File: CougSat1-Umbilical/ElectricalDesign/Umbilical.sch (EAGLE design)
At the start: 40 parts, among them Q1 CSD16406Q3, Q2 CSD16406Q3, U1 FT230XQ, U2 BQ24650

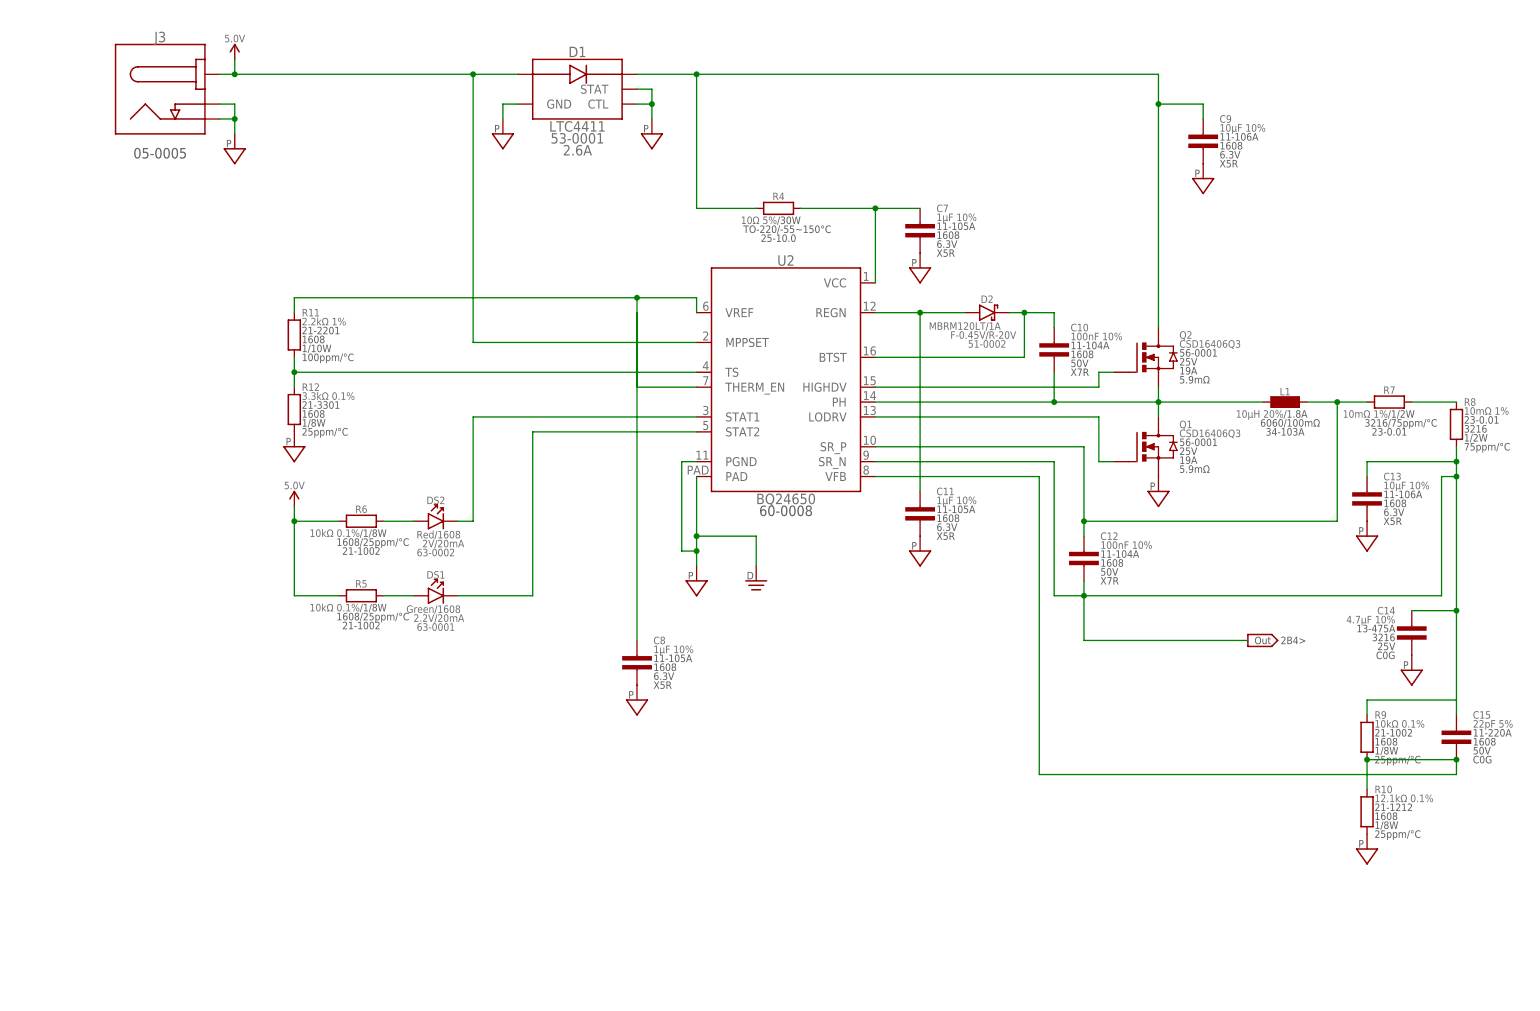
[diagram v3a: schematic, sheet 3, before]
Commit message: Update CougSat1-Umbilical/ElectricalDesign/Umbilical.sch
Fixed typing errors and cleaned up schmatic
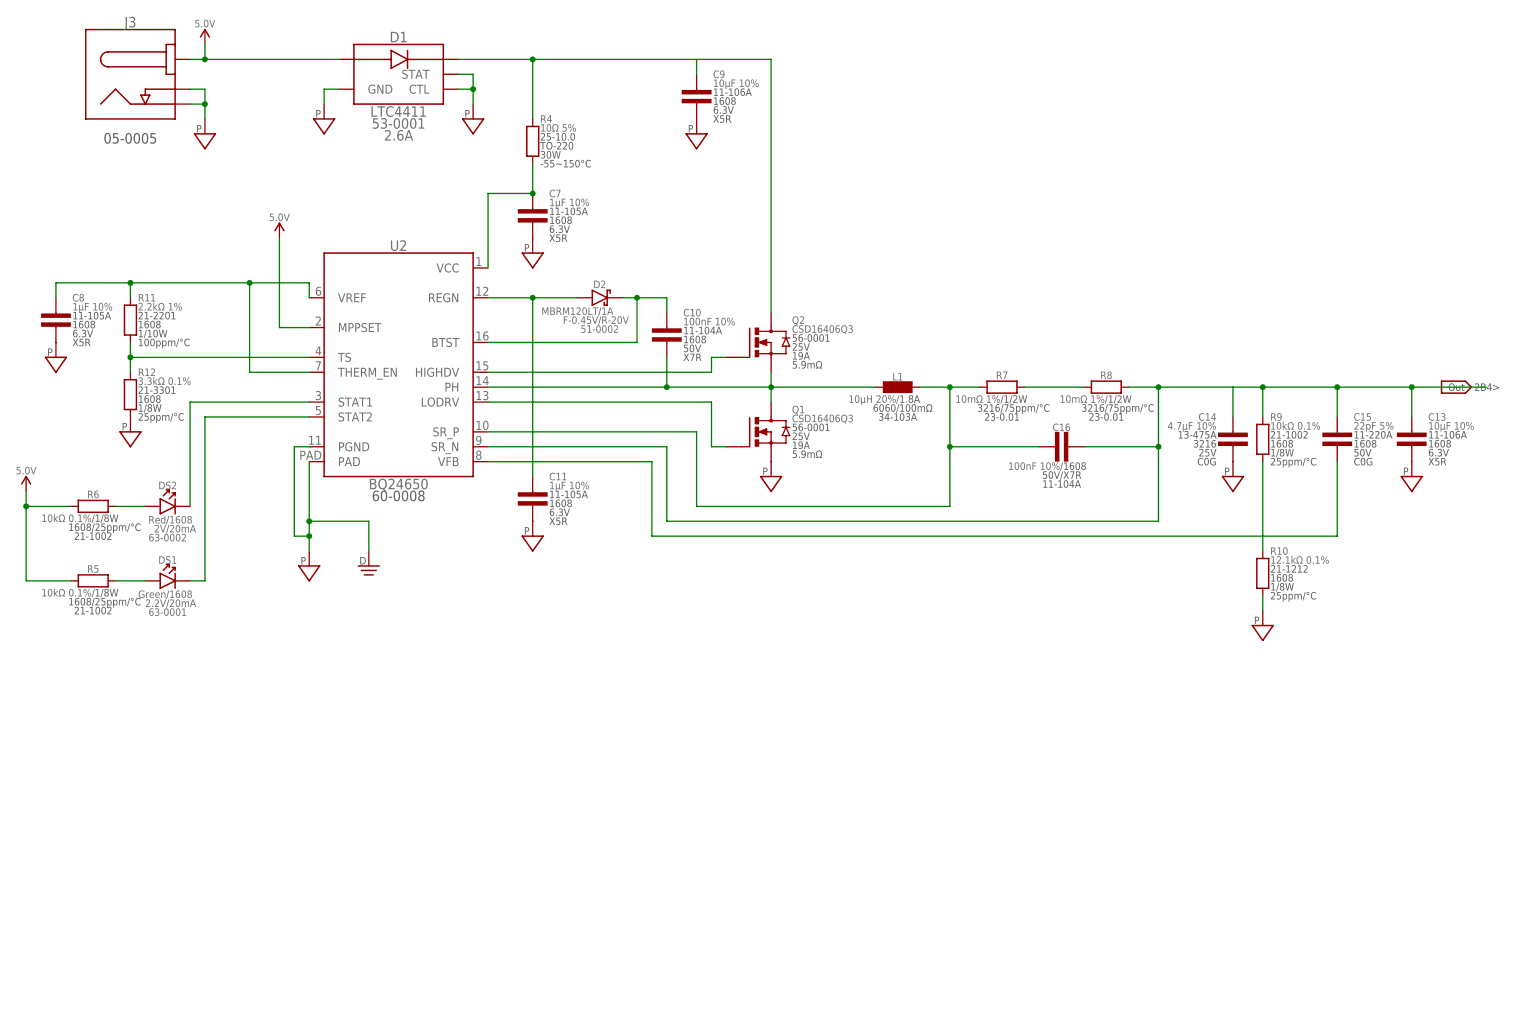
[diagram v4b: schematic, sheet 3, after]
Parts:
- removed C12: 100nF 10%, CougsInSpace-Capacitors:CAP-V-100NF-1608
- added C16: 100nF 10%, CougsInSpace-Capacitors:CAP-H-100NF-1608
- R4: device CougsInSpace-Resistors:RES-H-10R-TO220 -> CougsInSpace-Resistors:RES-V-10R-TO220
- R8: device CougsInSpace-Resistors:RES-V-0.01R-3216 -> CougsInSpace-Resistors:RES-H-0.01R-3216
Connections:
- removed net BARREL_MPPSET: D1.IN, J3.CENTER, U2.MPPSET
- removed net N$14: R7.2, R8.2
- removed net N$3: U2.THERM_EN
- new net N$1: C9.1
- new net N$2: R7.2, R8.1
- new net N$4: R10.2, R9.1
- net 5.0V: now also D1.IN, J3.CENTER, U2.MPPSET
- net BAT_CHARGE_OUT: now also C16.2, R8.2; no longer C12.2, R8.1
- net DIODE_OUT: now also R4.2; no longer C9.1, R4.1
- net SR_P: now also C16.1; no longer C12.1
- net VCC: now also R4.1; no longer R4.2
- net VFB: no longer R10.2, R9.1
- net VREF: now also U2.THERM_EN
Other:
- note added: "3B6>"
- note removed: "3C5>"
- moved on the sheet: C1, C10, C11, C13, C14, C15, C2, C3, C4, C5, C6, C7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

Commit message: Update CougSat1-Umbilical/ElectricalDesign/Umbilical.sch
1.0.1
Cleaned up schematic and changed resistors.
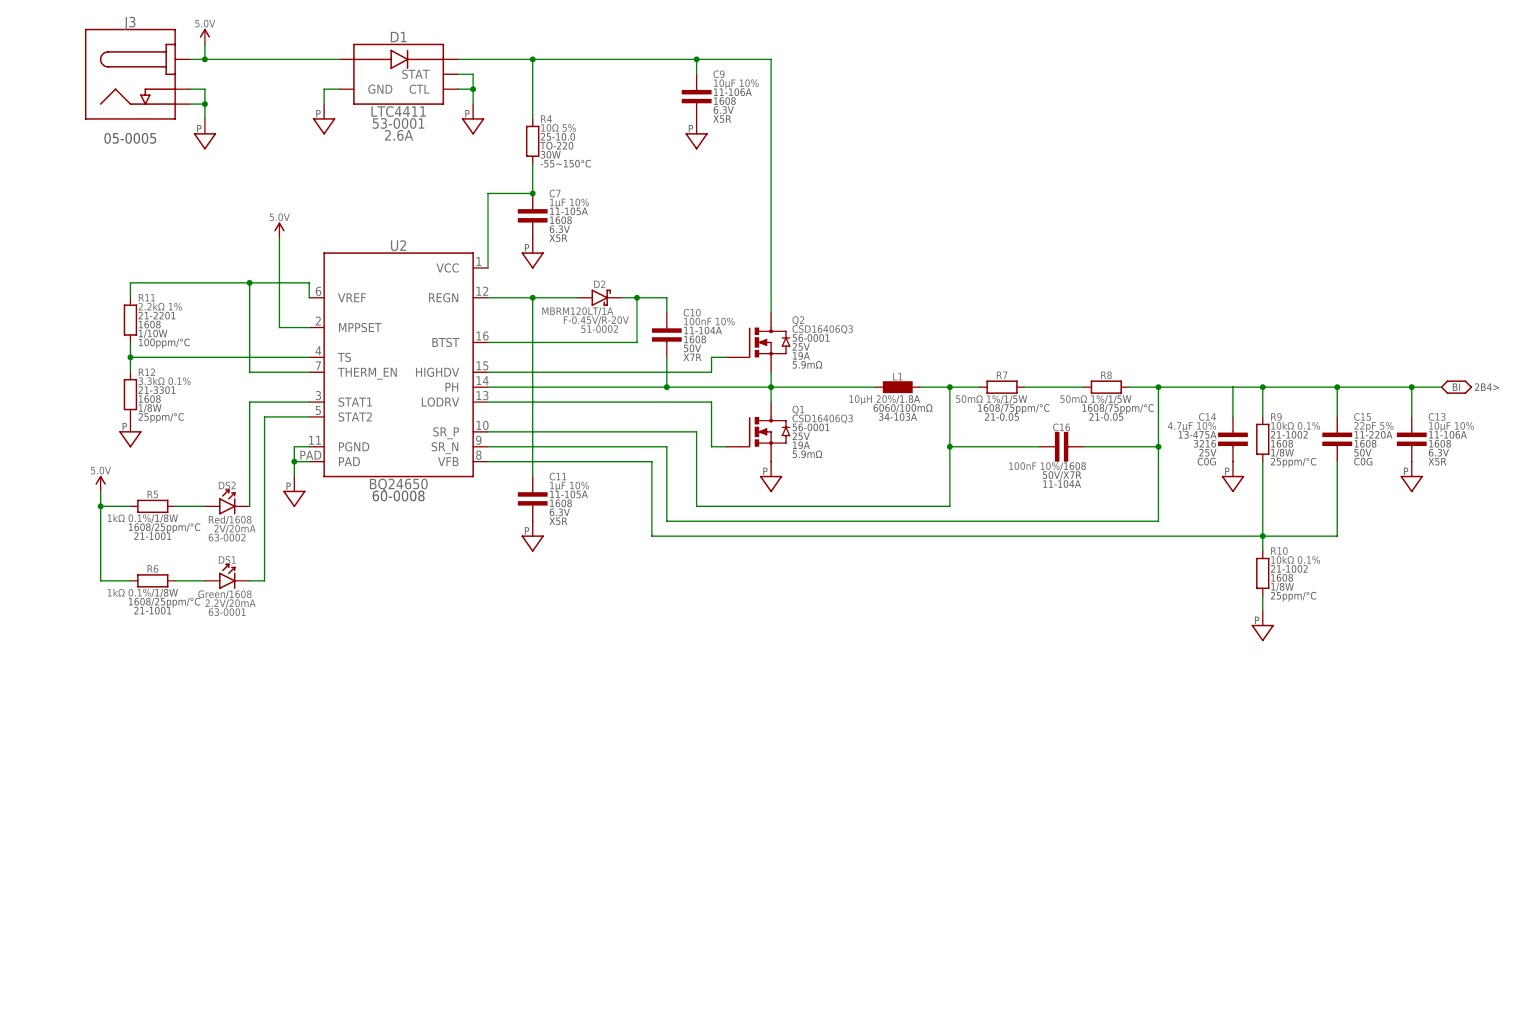
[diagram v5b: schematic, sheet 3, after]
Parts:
- removed C8: 1µF 10%, CougsInSpace-Capacitors:CAP-V-1UF-1608
- added C12: 100nF 10%, CougsInSpace-Capacitors:CAP-V-100NF-1608
- added R13: 0Ω <20mΩ, CougsInSpace-Resistors:RES-V-0-1608
- C6: value 4.7pF ±0.1 -> 4.7µF 10%; device CougsInSpace-Capacitors:CAP-V-4.7PF-1608 -> CougsInSpace-Capacitors:CAP-POL-V-4.7UF-4028
- R10: value 12.1kΩ 0.1% -> 10kΩ 0.1%; device CougsInSpace-Resistors:RES-V-12.1K-1608 -> CougsInSpace-Resistors:RES-V-10K-1608
- R5, R6: value 10kΩ 0.1% -> 1kΩ 0.1%; device CougsInSpace-Resistors:RES-H-10K-1608 -> CougsInSpace-Resistors:RES-H-1K-1608
- R7, R8: value 10mΩ 1% -> 50mΩ 1%; device CougsInSpace-Resistors:RES-H-0.01R-3216 -> CougsInSpace-Resistors:RES-H-0.05R-1608
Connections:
- removed net N$1: C9.1
- removed net N$4: R10.2, R9.1
- new net CHASSIS: C12.1, J1.SHIELD, R13.2
- net DGND: now also C12.2, C2.2, C3.2, C4.2, C5.2, C6.C, J1.GND, R13.1
- net DIODE_OUT: now also C9.1
- net N$7: now also R6.2; no longer R5.2
- net N$8: now also R5.2; no longer R6.2
- net PGND: no longer C2.2, C3.2, C4.2, C5.2, C6.2, C8.2, J1.GND, J1.SHIELD
- net USB5V_FILTERED: now also C6.A; no longer C6.1
- net VFB: now also R10.2, R9.1
- net VREF: no longer C8.1
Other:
- moved on the sheet: C2, C3, DS1, DS2, R5, R6

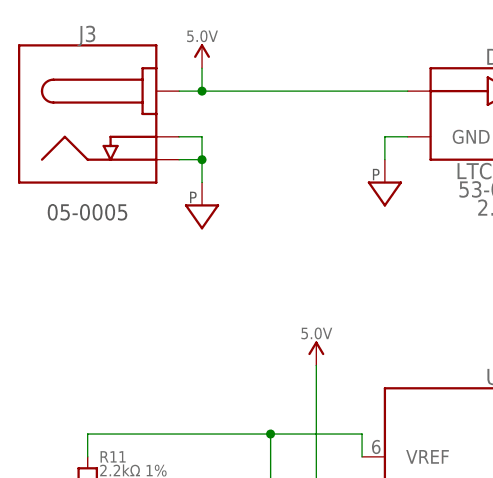
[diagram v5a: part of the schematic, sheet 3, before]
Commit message: Update CougSat1-Umbilical/ElectricalDesign/Umbilical.sch
1.0.2
Fixed value of J3
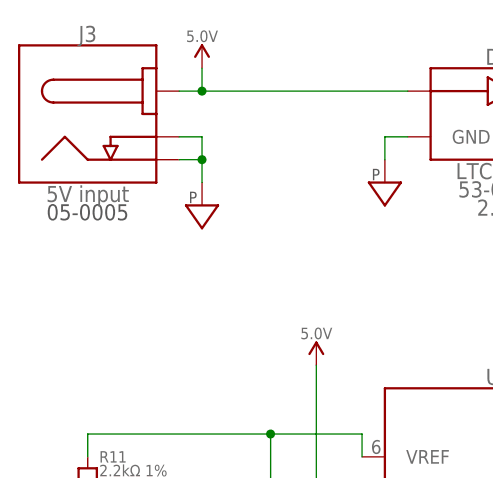
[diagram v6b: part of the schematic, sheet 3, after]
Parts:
- J3: value (none) -> 5V input
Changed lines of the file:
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@@
 <part name="C7" library="CougsInSpace-Capacitors" deviceset="CAP-V" device="-1608" technology="-1UF" value="1µF 10%"/>
 <part name="SUPPLY2" library="CougsInSpace-PowerSymbols" deviceset="PGND" device=""/>
-<part name="J3" library="CougsInSpace-Connectors" deviceset="BARREL" device="-2.1X5.5-R"/>
+<part name="J3" library="CougsInSpace-Connectors" deviceset="BARREL" device="-2.1X5.5-R" value="5V input"/>
 <part name="D1" library="CougsInSpace-DiscreteSemi" deviceset="LTC4411" device="" value="LTC4411"/>
 <part name="SUPPLY3" library="CougsInSpace-PowerSymbols" deviceset="PGND" device=""/>

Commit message: Added RC to reset and changed current sense resistor.
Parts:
- added C8: 100nF 10%, CougsInSpace-Capacitors:CAP-H-100NF-1608
- R7: value 50mΩ 1% -> 10kΩ 0.1%; device CougsInSpace-Resistors:RES-H-0.05R-1608 -> CougsInSpace-Resistors:RES-H-10K-1608
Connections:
- removed net N$2: R7.2, R8.1
- new net N$1: C8.1, R7.2, U1.!RESET
- net 3.3V: now also R7.1; no longer U1.!RESET
- net DGND: now also C8.2
- net SR_P: now also R8.1; no longer R7.1

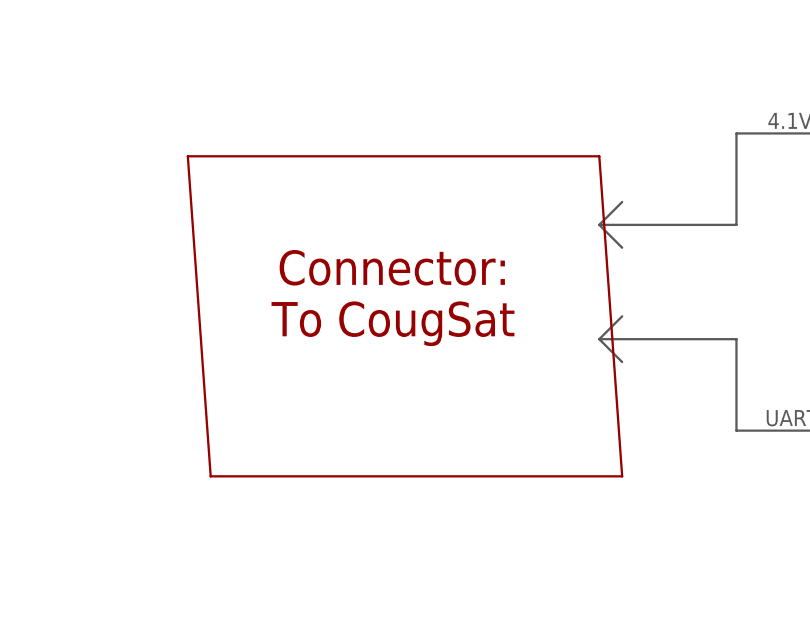
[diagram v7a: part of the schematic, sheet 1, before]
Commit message: update schematic
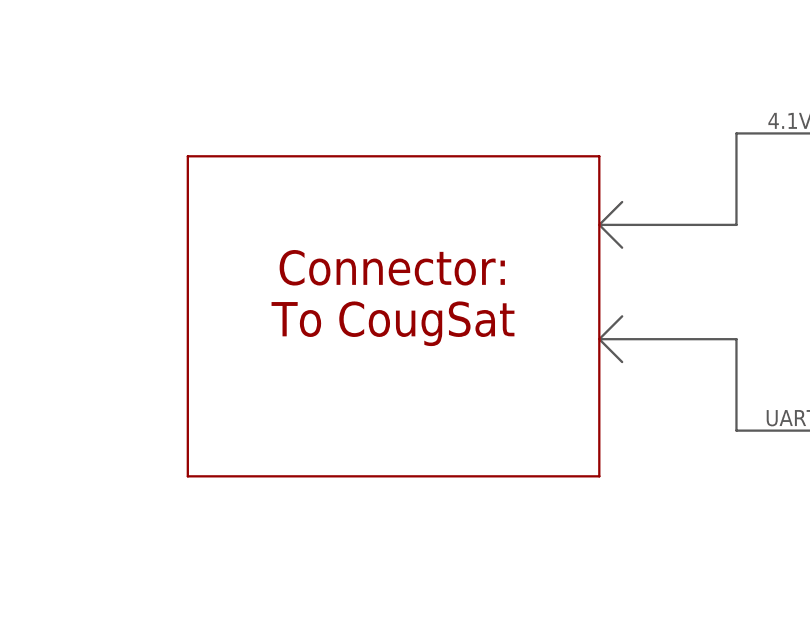
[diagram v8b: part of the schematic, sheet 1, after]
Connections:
- net N$7 renamed CHARGING_STAT_G_LED
- net N$8 renamed CHARGING_STAT_R_LED
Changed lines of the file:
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@@
 Page 3: Serial Transciever
 Page 4: Mechanical</text>
-<wire x1="30.48" y1="114.3" x2="33.02" y2="78.74" width="0.254" layer="94"/>
-<wire x1="33.02" y1="78.74" x2="78.74" y2="78.74" width="0.254" layer="94"/>
-<wire x1="78.74" y1="78.74" x2="76.2" y2="114.3" width="0.254" layer="94"/>
+<wire x1="30.48" y1="114.3" x2="30.48" y2="78.74" width="0.254" layer="94"/>
+<wire x1="30.48" y1="78.74" x2="76.2" y2="78.74" width="0.254" layer="94"/>
+<wire x1="76.2" y1="78.74" x2="76.2" y2="114.3" width="0.254" layer="94"/>
 <wire x1="76.2" y1="114.3" x2="30.48" y2="114.3" width="0.254" layer="94"/>
 <text x="53.34" y="99.06" size="3.81" layer="94" align="center">Connector:
@@
 </segment>
 </net>
-<net name="N$7" class="0">
+<net name="CHARGING_STAT_G_LED" class="0">
 <segment>
 <pinref part="DS1" gate="G$1" pin="A"/>
@@
 </segment>
 </net>
-<net name="N$8" class="0">
+<net name="CHARGING_STAT_R_LED" class="0">
 <segment>
 <pinref part="DS2" gate="G$1" pin="A"/>
